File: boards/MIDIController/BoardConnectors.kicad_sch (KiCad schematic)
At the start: 15 parts

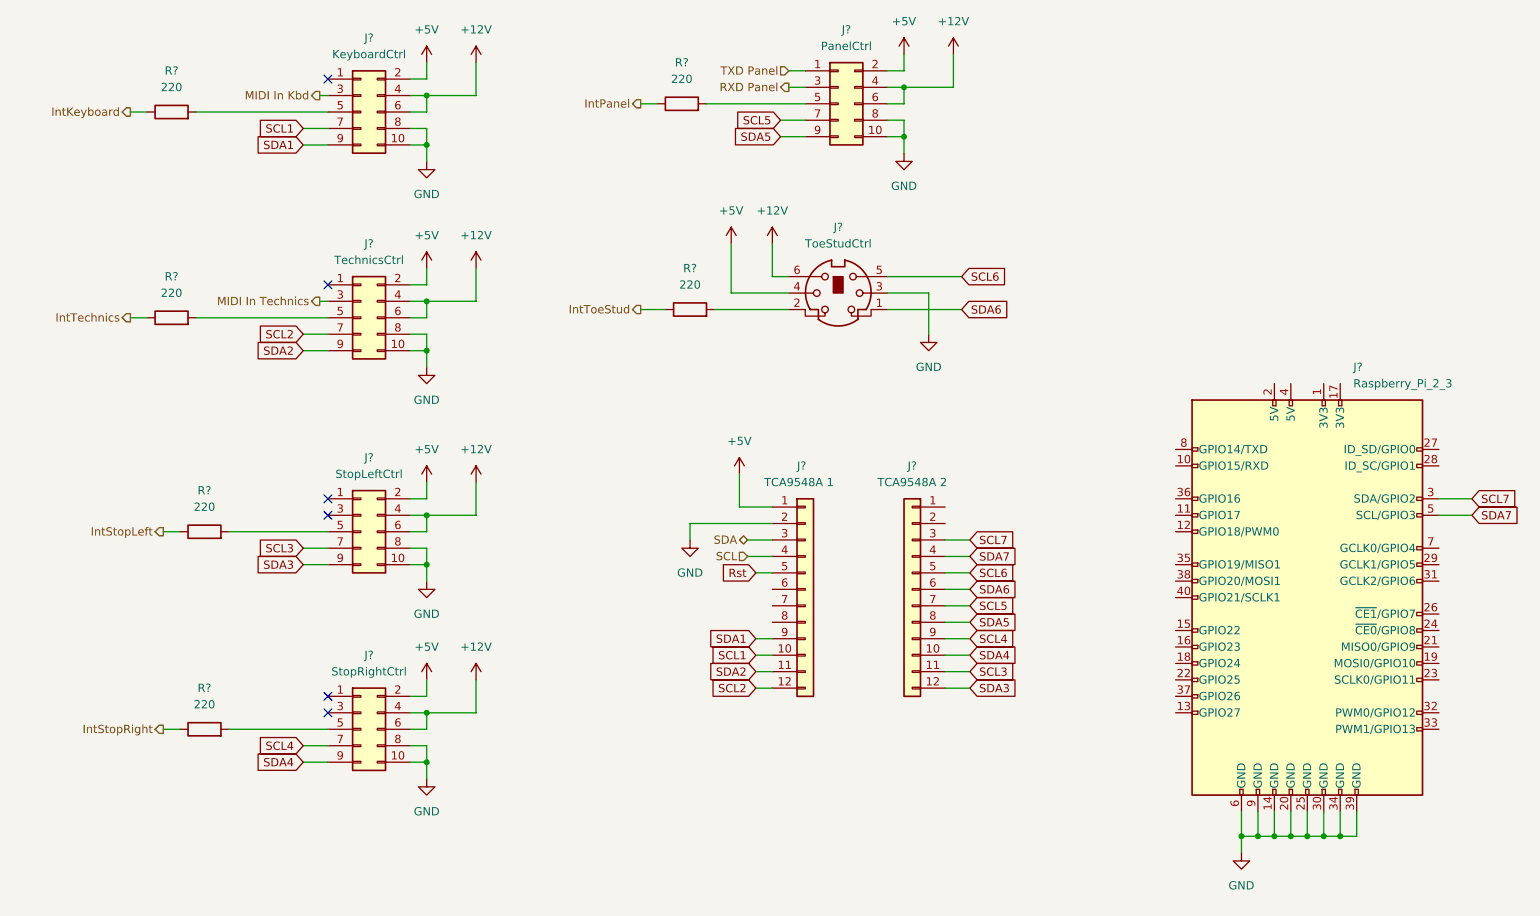
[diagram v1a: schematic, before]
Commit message: Cleanup of PCB sizes and mounthole positions. Moved MIDI connectors to separate board.
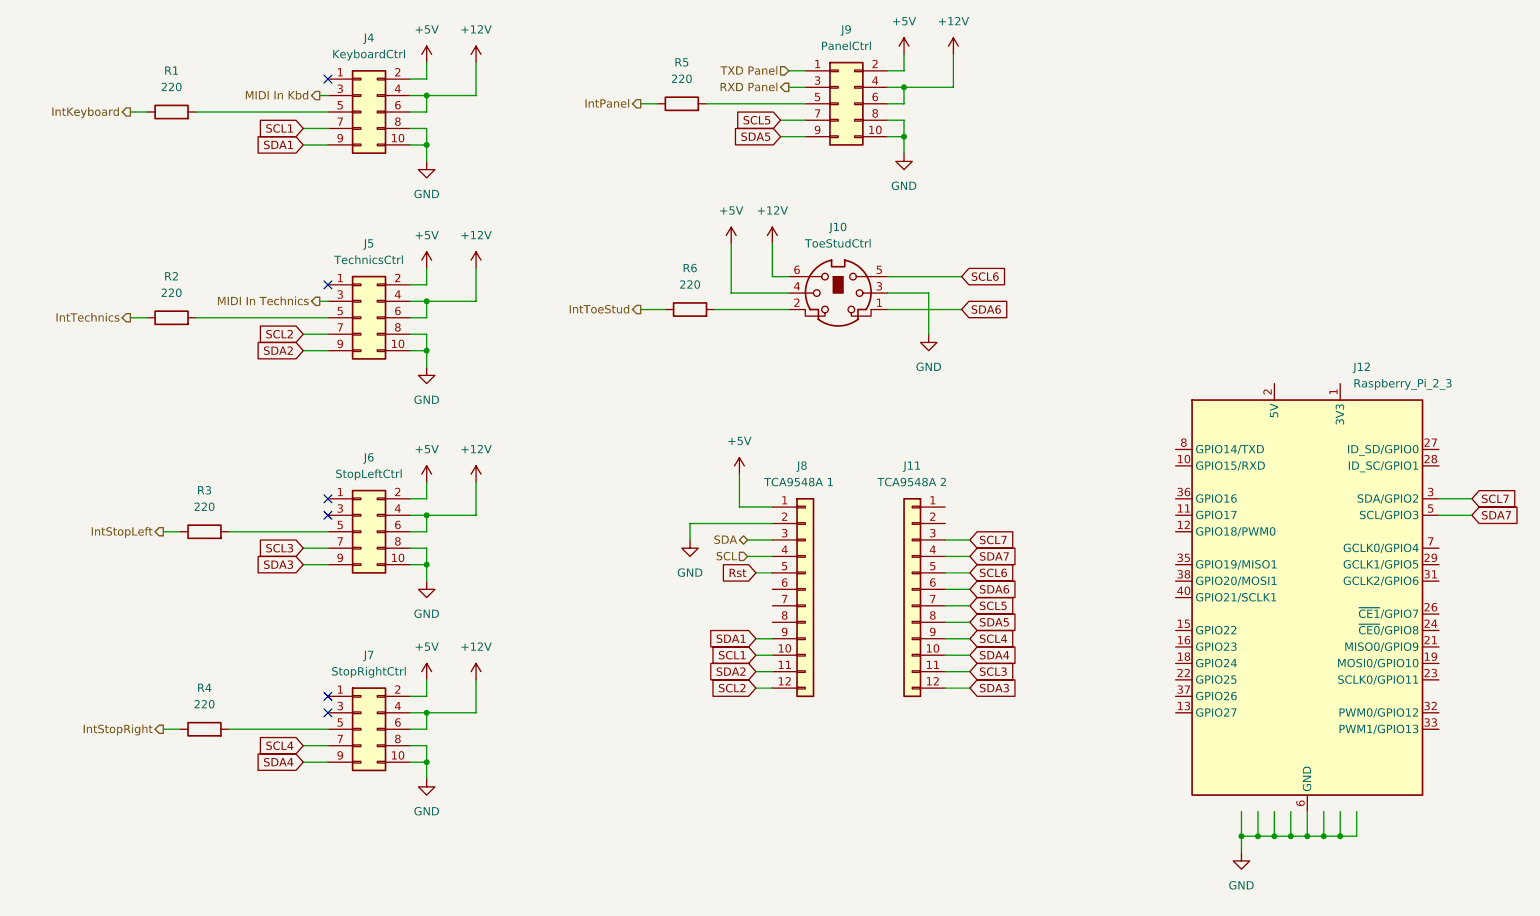
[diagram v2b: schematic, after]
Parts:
- gave numbers to parts that had none: 15
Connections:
- net at J12.1 (3V3): now also J12.17 (3V3)
- net at J12.2 (5V): now also J12.4 (5V)

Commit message: Added Optocoupler and RS232 converter to UART board lines.
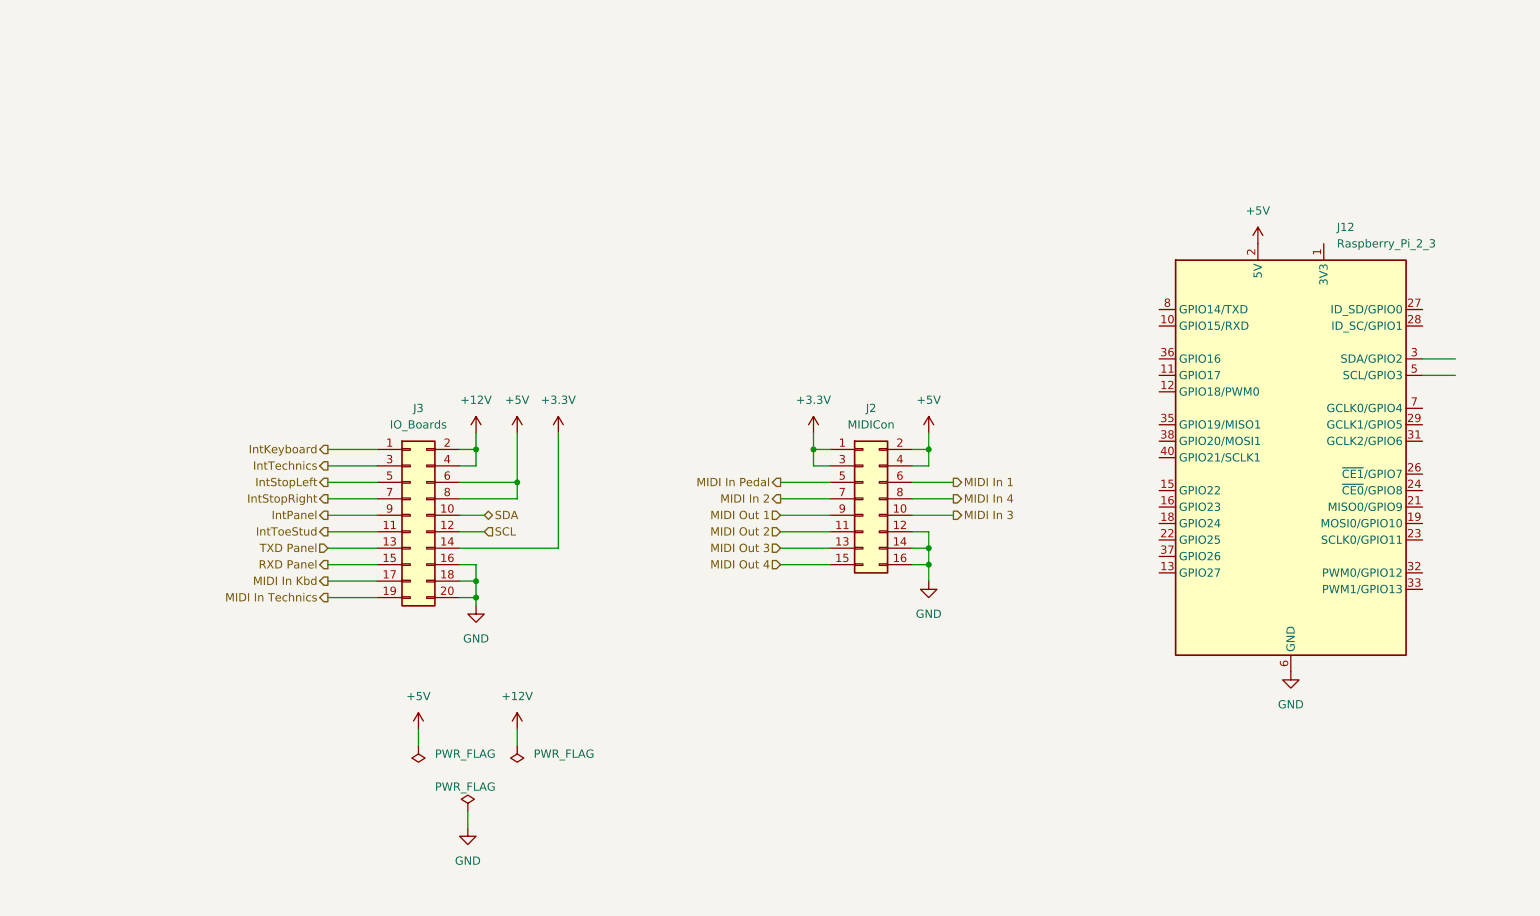
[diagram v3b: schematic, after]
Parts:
- removed J10: ToeStudCtrl, symbol Connector:Mini-DIN-6
- removed J11: TCA9548A 2, symbol Connector_Generic:Conn_01x12
- removed J4: KeyboardCtrl, Connector_IDC:IDC-Header_2x05_P2.54mm_Vertical, symbol Connector_Generic:Conn_02x05_Odd_Even
- removed J5: TechnicsCtrl, Connector_IDC:IDC-Header_2x05_P2.54mm_Vertical, symbol Connector_Generic:Conn_02x05_Odd_Even
- removed J6: StopLeftCtrl, Connector_IDC:IDC-Header_2x05_P2.54mm_Vertical, symbol Connector_Generic:Conn_02x05_Odd_Even
- removed J7: StopRightCtrl, Connector_IDC:IDC-Header_2x05_P2.54mm_Vertical, symbol Connector_Generic:Conn_02x05_Odd_Even
- removed J8: TCA9548A 1, symbol Connector_Generic:Conn_01x12
- removed J9: PanelCtrl, Connector_IDC:IDC-Header_2x05_P2.54mm_Vertical, symbol Connector_Generic:Conn_02x05_Odd_Even
- removed R1, R2, R3, R4, R5, R6: 220, Resistor_THT:R_Axial_DIN0204_L3.6mm_D1.6mm_P2.54mm_Vertical, symbol Device:R
- added J2: MIDICon, Connector_IDC:IDC-Header_2x08_P2.54mm_Vertical, symbol Connector_Generic:Conn_02x08_Odd_Even
- added J3: IO_Boards, Connector_IDC:IDC-Header_2x10_P2.54mm_Vertical, symbol Connector_Generic:Conn_02x10_Odd_Even
- J12: footprint (none) -> Connector_PinHeader_2.54mm:PinHeader_2x20_P2.54mm_Vertical
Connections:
- net +12V: now also J3.2 (Pin_2), J3.4 (Pin_4)
- net +5V: now also J12.2 (5V), J12.4 (5V), J2.2 (Pin_2), J2.4 (Pin_4), J3.6 (Pin_6), J3.8 (Pin_8)
- net GND: now also J2.12 (Pin_12), J2.14 (Pin_14), J2.16 (Pin_16), J3.16 (Pin_16), J3.18 (Pin_18), J3.20 (Pin_20)
- net IntKeyboard: now also J3.1 (Pin_1)
- net IntPanel: now also J3.9 (Pin_9)
- net IntStopLeft: now also J3.5 (Pin_5)
- net IntStopRight: now also J3.7 (Pin_7)
- net IntTechnics: now also J3.3 (Pin_3)
- net IntToeStud: now also J3.11 (Pin_11)
- net MIDI In Kbd: now also J3.17 (Pin_17)
- net MIDI In Technics: now also J3.19 (Pin_19)
- net RXD Panel: now also J3.15 (Pin_15)
- net SCL: now also J3.12 (Pin_12)
- net SDA: now also J3.10 (Pin_10)
- net TXD Panel: now also J3.13 (Pin_13)
- net SCL7: no longer names the net of J12.3 (SDA/GPIO2)
- net SDA7: no longer names the net of J12.5 (SCL/GPIO3)
- new net +3.3V: J2.1 (Pin_1), J2.3 (Pin_3), J3.14 (Pin_14)
- new net MIDI In 1: J2.6 (Pin_6)
- new net MIDI In 2: J2.7 (Pin_7)
- new net MIDI In 3: J2.10 (Pin_10)
- new net MIDI In 4: J2.8 (Pin_8)
- new net MIDI In Pedal: J2.5 (Pin_5)
- new net MIDI Out 1: J2.9 (Pin_9)
- new net MIDI Out 2: J2.11 (Pin_11)
- new net MIDI Out 3: J2.13 (Pin_13)
- new net MIDI Out 4: J2.15 (Pin_15)
- no-connect marks 6 -> 0
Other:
- moved on the sheet: J12

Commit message: Finished connectors on MIDIController board, fixed 3.3V IO voltage levels
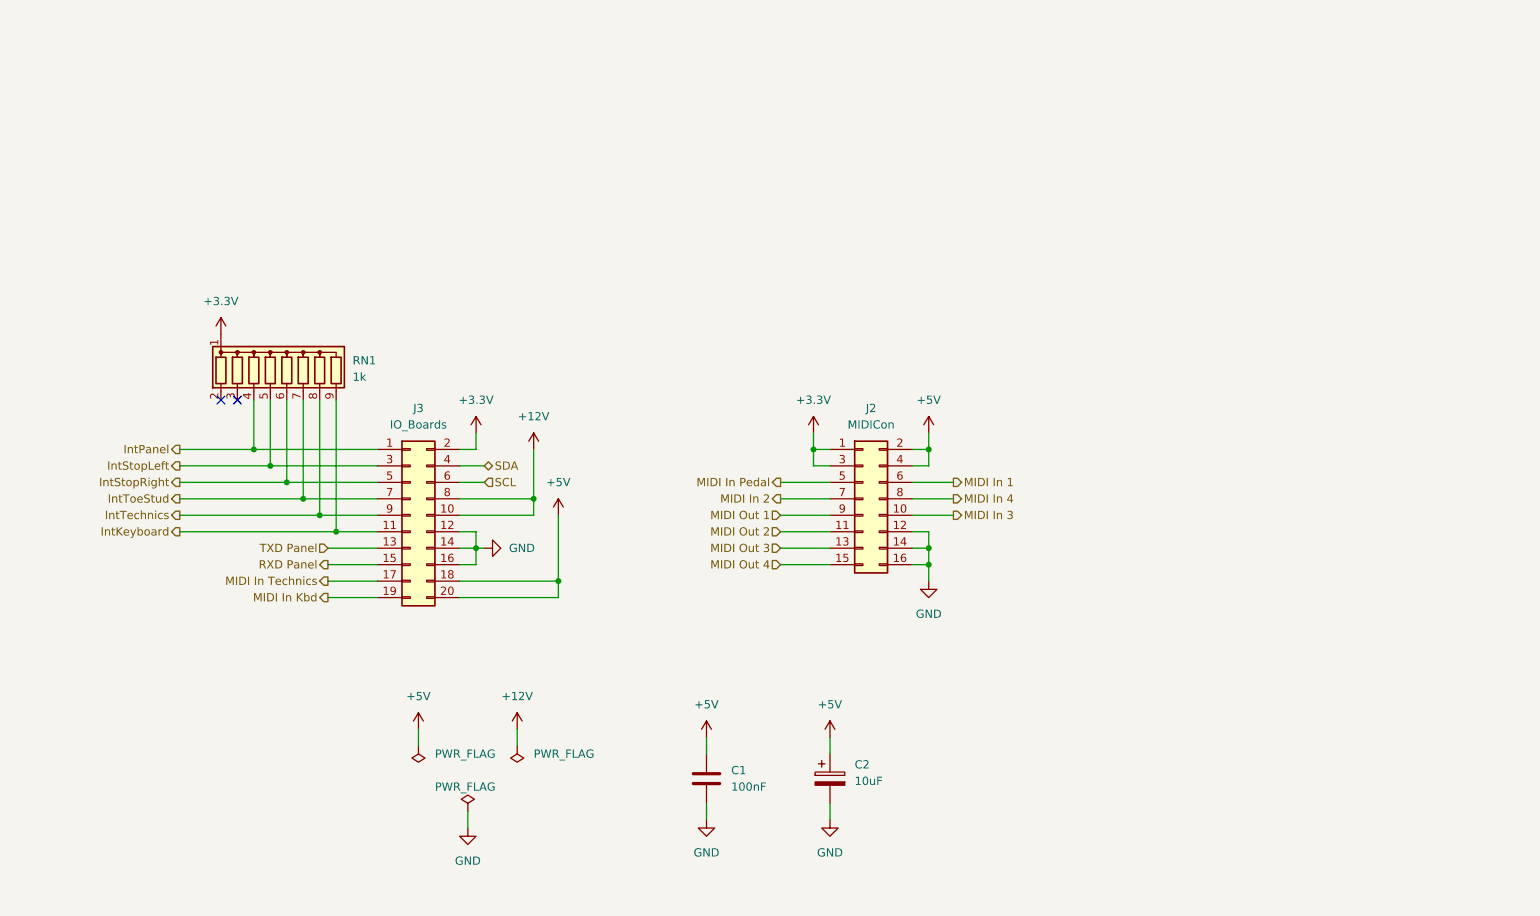
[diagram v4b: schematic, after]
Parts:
- removed J12: Raspberry_Pi_2_3, Connector_PinHeader_2.54mm:PinHeader_2x20_P2.54mm_Vertical, symbol Connector:Raspberry_Pi_2_3
- added C1: 100nF, symbol Device:C
- added C2: 10uF, symbol Device:C_Polarized
- added RN1: 1k, Resistor_THT:R_Array_SIP9, symbol Device:R_Network08
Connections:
- net +12V: now also J3.10 (Pin_10), J3.8 (Pin_8); no longer J3.2 (Pin_2), J3.4 (Pin_4)
- net +3.3V: now also J3.2 (Pin_2), RN1.1 (common); no longer J3.14 (Pin_14)
- net +5V: now also J3.18 (Pin_18), J3.20 (Pin_20), C1.1, C2.1; no longer J3.6 (Pin_6), J3.8 (Pin_8)
- net GND: now also J3.12 (Pin_12), J3.14 (Pin_14), C1.2, C2.2; no longer J3.18 (Pin_18), J3.20 (Pin_20)
- net IntKeyboard: now also J3.11 (Pin_11), RN1.9 (R8); no longer J3.1 (Pin_1)
- net IntPanel: now also J3.1 (Pin_1), RN1.4 (R3); no longer J3.9 (Pin_9)
- net IntStopLeft: now also J3.3 (Pin_3), RN1.5 (R4); no longer J3.5 (Pin_5)
- net IntStopRight: now also J3.5 (Pin_5), RN1.6 (R5); no longer J3.7 (Pin_7)
- net IntTechnics: now also J3.9 (Pin_9), RN1.8 (R7); no longer J3.3 (Pin_3)
- net IntToeStud: now also J3.7 (Pin_7), RN1.7 (R6); no longer J3.11 (Pin_11)
- net MIDI In Kbd: now also J3.19 (Pin_19); no longer J3.17 (Pin_17)
- net MIDI In Technics: now also J3.17 (Pin_17); no longer J3.19 (Pin_19)
- net SCL: now also J3.6 (Pin_6); no longer J3.12 (Pin_12)
- net SDA: now also J3.4 (Pin_4); no longer J3.10 (Pin_10)
- no-connect marks 0 -> 2

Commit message: Updated MidiController PCB footprints
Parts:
- C1: footprint (none) -> Capacitor_THT:C_Disc_D4.3mm_W1.9mm_P5.00mm
- C2: footprint (none) -> Capacitor_THT:CP_Radial_D7.5mm_P2.50mm
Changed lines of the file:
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@@
 			)
 		)
-		(property "Footprint" ""
+		(property "Footprint" "Capacitor_THT:CP_Radial_D7.5mm_P2.50mm"
 			(at 157.1752 146.05 0)
 			(effects
@@
 			)
 		)
-		(property "Footprint" ""
+		(property "Footprint" "Capacitor_THT:C_Disc_D4.3mm_W1.9mm_P5.00mm"
 			(at 138.1252 146.05 0)
 			(effects
